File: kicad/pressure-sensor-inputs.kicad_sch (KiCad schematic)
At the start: 10 parts

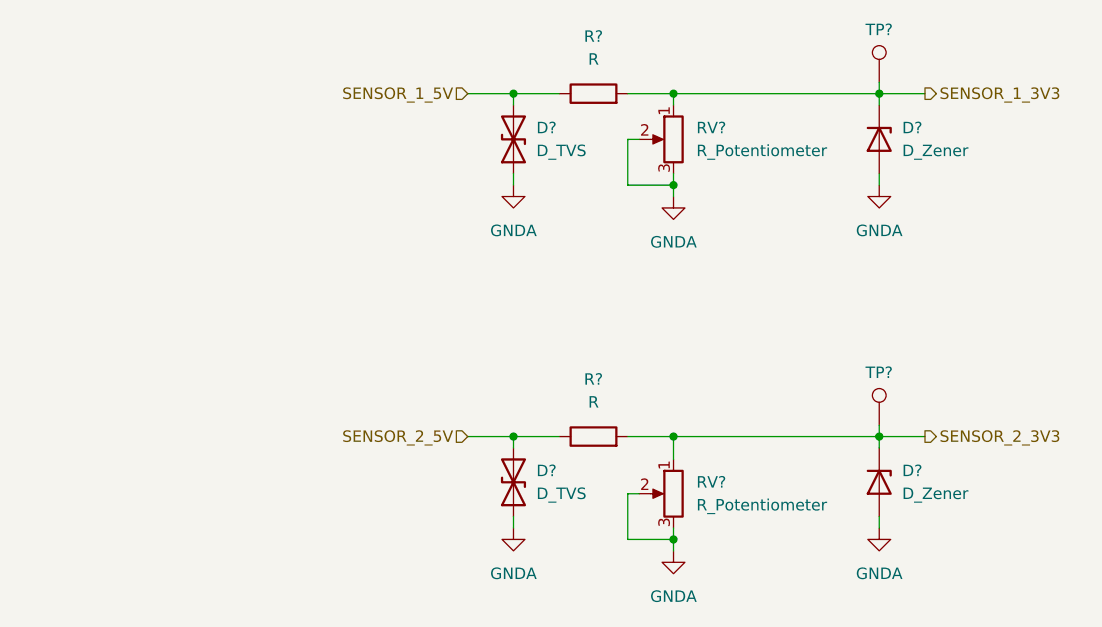
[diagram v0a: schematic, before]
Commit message: Update ADC input divider and protection
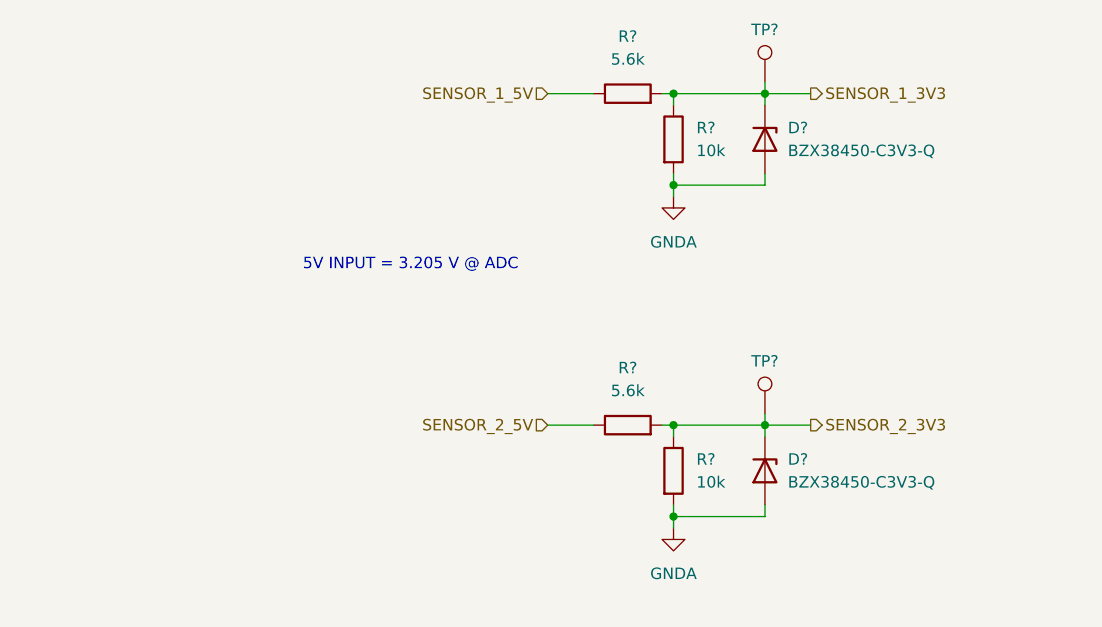
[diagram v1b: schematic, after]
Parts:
- removed D?: D_Zener, symbol symbols:D_Zener
- removed D? (x2): D_TVS, symbol bmw-e36-abs-module:D_TVS
- removed R?: R, symbol symbols:R
- removed RV? (x2): R_Potentiometer, symbol symbols:R_Potentiometer
- removed TP?: TestPoint, symbol symbols:TestPoint
- added D?: BZX38450-C3V3-Q, Diode_SMD:D_SOD-323, symbol symbols:D_Zener
- added R? (x2): 10k, symbol symbols:R
- added R?: 5.6k, symbol symbols:R
- added TP?: TestPoint, symbol symbols:TestPoint
- D?: value D_Zener -> BZX38450-C3V3-Q; footprint (none) -> Diode_SMD:D_SOD-323; Manufacturer (none) -> Nexperia; Part Number (none) -> BZX38450-C3V3-Q
- R?: value R -> 5.6k
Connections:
- net GNDA: now also D?.2 (A), R?.2, R?.2
- net SENSOR_1_3V3: now also R?.1
- net SENSOR_2_3V3: now also D?.1 (K), R?.1, R?.2, TP?.1
- net SENSOR_2_5V: now also R?.1
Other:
- note added: "5V INPUT = 3.205 V @ ADC"
- moved on the sheet: D?, R?, TP?

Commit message: Update connector; annotate and assign footprints
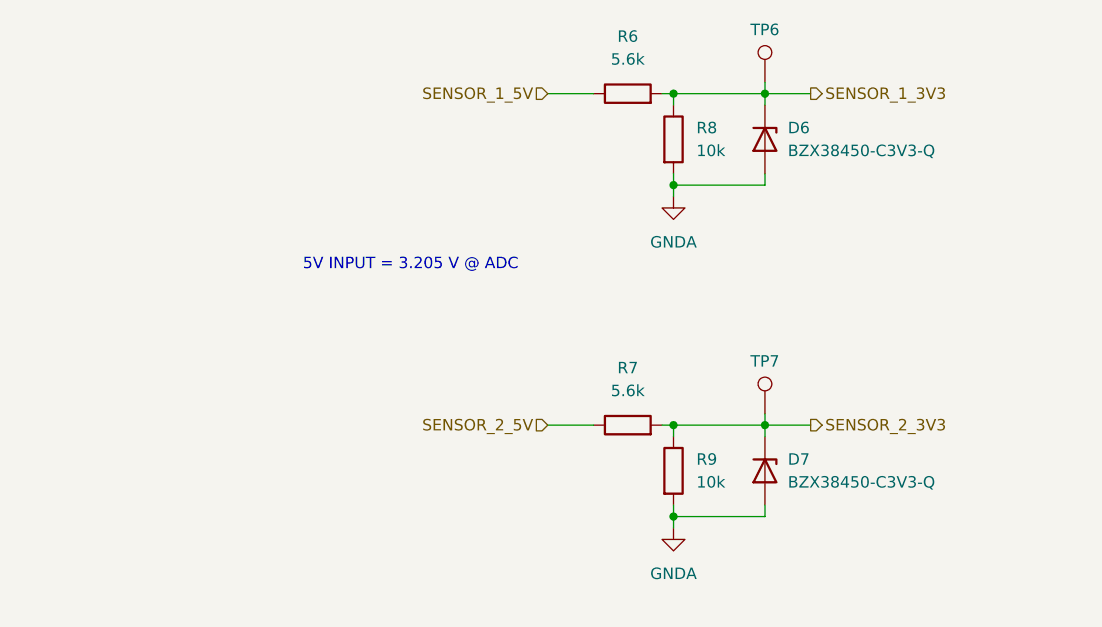
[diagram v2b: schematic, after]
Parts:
- R6, R7, R8, R9: renamed from R?; footprint (none) -> Resistor_SMD:R_0603_1608Metric
- TP6, TP7: renamed from TP?; footprint (none) -> TestPoint:TestPoint_Pad_D2.0mm
- gave numbers to parts that had none: 2
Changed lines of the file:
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@@
 		(dnp no)
 		(fields_autoplaced yes)
-		(property "Reference" "R?"
+		(property "Reference" "R8"
 			(at 208.28 111.7599 0)
 			(show_name no)
@@
 			)
 		)
-		(property "Footprint" ""
+		(property "Footprint" "Resistor_SMD:R_0603_1608Metric"
 			(at 203.962 113.03 90)
 			(hide yes)
@@
 			(project "bmw-e36-abs-adapter"
 				(path "/325be93f-b4a6-4f2b-83c3-2ccd33e5cc03/18849697-e921-4429-b50d-ca2a9ec17916"
-					(reference "R?")
+					(reference "R8")
 					(unit 1)
 				)
@@
 		(in_pos_files yes)
 		(dnp no)
-		(property "Reference" "TP?"
+		(property "Reference" "TP6"
 			(at 215.9 101.6 0)
 			(show_name no)
@@
 			)
 		)
-		(property "Footprint" ""
+		(property "Footprint" "TestPoint:TestPoint_Pad_D2.0mm"
 			(at 210.82 106.68 0)
 			(hide yes)
@@
 			(project "bmw-e36-abs-adapter"
 				(path "/325be93f-b4a6-4f2b-83c3-2ccd33e5cc03/18849697-e921-4429-b50d-ca2a9ec17916"
-					(reference "TP?")
+					(reference "TP6")
 					(unit 1)
 				)
@@
 		(dnp no)
 		(fields_autoplaced yes)
-		(property "Reference" "D?"
+		(property "Reference" "D7"
 			(at 218.44 148.5899 90)
 			(show_name no)
@@
 			(project "bmw-e36-abs-adapter"
 				(path "/325be93f-b4a6-4f2b-83c3-2ccd33e5cc03/18849697-e921-4429-b50d-ca2a9ec17916"
-					(reference "D?")
+					(reference "D7")
 					(unit 1)
 				)
@@
 		(dnp no)
 		(fields_autoplaced yes)
-		(property "Reference" "R?"
+		(property "Reference" "R9"
 			(at 208.28 148.5899 0)
 			(show_name no)
@@
 			)
 		)
-		(property "Footprint" ""
+		(property "Footprint" "Resistor_SMD:R_0603_1608Metric"
 			(at 203.962 149.86 90)
 			(hide yes)
@@
 			(project "bmw-e36-abs-adapter"
 				(path "/325be93f-b4a6-4f2b-83c3-2ccd33e5cc03/18849697-e921-4429-b50d-ca2a9ec17916"
-					(reference "R?")
+					(reference "R9")
 					(unit 1)
 				)
@@
 		(dnp no)
 		(fields_autoplaced yes)
-		(property "Reference" "R?"
+		(property "Reference" "R6"
 			(at 200.66 101.6 90)
 			(show_name no)
@@
 			)
 		)
-		(property "Footprint" ""
+		(property "Footprint" "Resistor_SMD:R_0603_1608Metric"
 			(at 200.66 109.728 90)
 			(hide yes)
@@
 			(project "bmw-e36-abs-adapter"
 				(path "/325be93f-b4a6-4f2b-83c3-2ccd33e5cc03/18849697-e921-4429-b50d-ca2a9ec17916"
-					(reference "R?")
+					(reference "R6")
 					(unit 1)
 				)
@@
 		(dnp no)
 		(fields_autoplaced yes)
-		(property "Reference" "D?"
+		(property "Reference" "D6"
 			(at 218.44 111.7599 90)
 			(show_name no)
@@
 			(project "bmw-e36-abs-adapter"
 				(path "/325be93f-b4a6-4f2b-83c3-2ccd33e5cc03/18849697-e921-4429-b50d-ca2a9ec17916"
-					(reference "D?")
+					(reference "D6")
 					(unit 1)
 				)
@@
 		(in_pos_files yes)
 		(dnp no)
-		(property "Reference" "TP?"
+		(property "Reference" "TP7"
 			(at 215.9 138.43 0)
 			(show_name no)
@@
 			)
 		)
-		(property "Footprint" ""
+		(property "Footprint" "TestPoint:TestPoint_Pad_D2.0mm"
 			(at 210.82 143.51 0)
 			(hide yes)
@@
 			(project "bmw-e36-abs-adapter"
 				(path "/325be93f-b4a6-4f2b-83c3-2ccd33e5cc03/18849697-e921-4429-b50d-ca2a9ec17916"
-					(reference "TP?")
+					(reference "TP7")
 					(unit 1)
 				)
@@
 		(dnp no)
 		(fields_autoplaced yes)
-		(property "Reference" "R?"
+		(property "Reference" "R7"
 			(at 200.66 138.43 90)
 			(show_name no)
@@
 			)
 		)
-		(property "Footprint" ""
+		(property "Footprint" "Resistor_SMD:R_0603_1608Metric"
 			(at 200.66 146.558 90)
 			(hide yes)
@@
 			(project "bmw-e36-abs-adapter"
 				(path "/325be93f-b4a6-4f2b-83c3-2ccd33e5cc03/18849697-e921-4429-b50d-ca2a9ec17916"
-					(reference "R?")
+					(reference "R7")
 					(unit 1)
 				)
@@
 		(dnp no)
 		(fields_autoplaced yes)
-		(property "Reference" "#PWR?"
+		(property "Reference" "#PWR034"
 			(at 205.74 125.73 0)
 			(hide yes)
@@
 			(project "bmw-e36-abs-adapter"
 				(path "/325be93f-b4a6-4f2b-83c3-2ccd33e5cc03/18849697-e921-4429-b50d-ca2a9ec17916"
-					(reference "#PWR?")
+					(reference "#PWR034")
 					(unit 1)
 				)
@@
 		(dnp no)
 		(fields_autoplaced yes)
-		(property "Reference" "#PWR?"
+		(property "Reference" "#PWR035"
 			(at 205.74 162.56 0)
 			(hide yes)
@@
 			(project "bmw-e36-abs-adapter"
 				(path "/325be93f-b4a6-4f2b-83c3-2ccd33e5cc03/18849697-e921-4429-b50d-ca2a9ec17916"
-					(reference "#PWR?")
-					(unit 1)
-				)
+					(reference "#PWR035")
+					(unit 1)
+				)

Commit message: Add optional RC filter to pressure sensor inputs
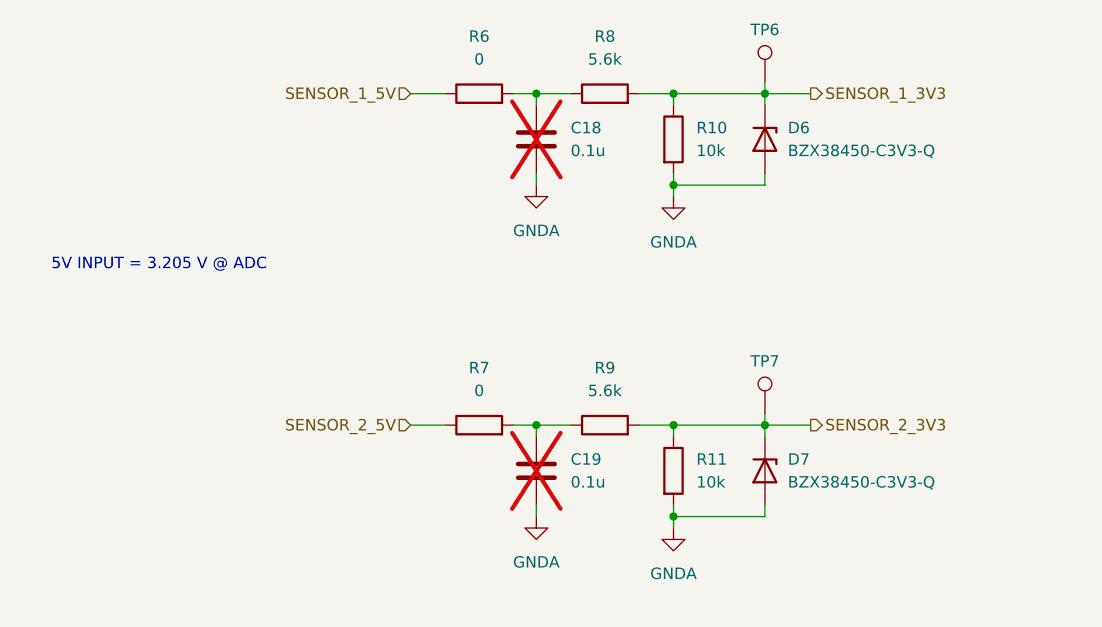
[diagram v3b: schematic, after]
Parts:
- added C18, C19: 0.1u, Capacitor_SMD:C_0603_1608Metric, symbol symbols:C
- added R6, R7: 0, Resistor_SMD:R_0603_1608Metric, symbol symbols:R
- renumbered R8 to R10, R9 to R11, R6 to R8, R7 to R9
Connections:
- net GNDA: now also C18.2, C19.2
- net SENSOR_1_5V: now also R6.1; no longer R8.1
- net SENSOR_2_5V: now also R7.1; no longer R9.1
- new net: C19.1, R7.2, R9.1
- new net: C18.1, R6.2, R8.1
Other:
- moved on the sheet: R8, R9

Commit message: Update part numbers and fix ERC issues
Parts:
- C18, C19: Manufacturer (none) -> Murata; Part Number (none) -> GCJ188R71H104KA12D; now left out of the parts list
- R10, R11: Manufacturer (none) -> Panasonic; Part Number (none) -> ERJ-3EKF1002V
- R6, R7: Manufacturer (none) -> Panasonic; Part Number (none) -> ERJ-H3G0R00V
- R8, R9: Manufacturer (none) -> Panasonic; Part Number (none) -> ERJ-3EKF5601V
- TP6, TP7: now left out of the parts list
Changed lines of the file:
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@@
+			)
+		)
+		(property "Manufacturer" "Panasonic"
+			(at 205.74 113.03 0)
+			(hide yes)
+			(show_name no)
+			(do_not_autoplace no)
+			(effects
+				(font
+					(size 1.27 1.27)
+				)
+			)
+		)
+		(property "Part Number" "ERJ-3EKF1002V"
+			(at 205.74 113.03 0)
+			(hide yes)
+			(show_name no)
+			(do_not_autoplace no)
+			(effects
+				(font
+					(size 1.27 1.27)
+				)
 			)
 		)
@@
 		(body_style 1)
 		(exclude_from_sim no)
-		(in_bom yes)
+		(in_bom no)
 		(on_board yes)
 		(in_pos_files yes)
@@
 		)
 		(property "Description" "Unpolarized capacitor"
+			(at 190.5 149.86 0)
+			(hide yes)
+			(show_name no)
+			(do_not_autoplace no)
+			(effects
+				(font
+					(size 1.27 1.27)
+				)
+			)
+		)
+		(property "Manufacturer" "Murata"
+			(at 190.5 149.86 0)
+			(hide yes)
+			(show_name no)
+			(do_not_autoplace no)
+			(effects
+				(font
+					(size 1.27 1.27)
+				)
+			)
+		)
+		(property "Part Number" "GCJ188R71H104KA12D"
 			(at 190.5 149.86 0)
 			(hide yes)
@@
 		(body_style 1)
 		(exclude_from_sim no)
-		(in_bom yes)
+		(in_bom no)
 		(on_board yes)
 		(in_pos_files yes)
@@
 		)
 		(property "Description" "Unpolarized capacitor"
+			(at 190.5 113.03 0)
+			(hide yes)
+			(show_name no)
+			(do_not_autoplace no)
+			(effects
+				(font
+					(size 1.27 1.27)
+				)
+			)
+		)
+		(property "Manufacturer" "Murata"
+			(at 190.5 113.03 0)
+			(hide yes)
+			(show_name no)
+			(do_not_autoplace no)
+			(effects
+				(font
+					(size 1.27 1.27)
+				)
+			)
+		)
+		(property "Part Number" "GCJ188R71H104KA12D"
 			(at 190.5 113.03 0)
 			(hide yes)
@@
 		(body_style 1)
 		(exclude_from_sim no)
-		(in_bom yes)
+		(in_bom no)
 		(on_board yes)
 		(in_pos_files yes)
@@
 			)
 		)
+		(property "Manufacturer" "Panasonic"
+			(at 205.74 149.86 0)
+			(hide yes)
+			(show_name no)
+			(do_not_autoplace no)
+			(effects
+				(font
+					(size 1.27 1.27)
+				)
+			)
+		)
+		(property "Part Number" "ERJ-3EKF1002V"
+			(at 205.74 149.86 0)
+			(hide yes)
+			(show_name no)
+			(do_not_autoplace no)
+			(effects
+				(font
+					(size 1.27 1.27)
+				)
+			)
+		)
 		(pin "1"
 		)
@@
 			)
 		)
+		(property "Manufacturer" "Panasonic"
+			(at 184.15 144.78 90)
+			(hide yes)
+			(show_name no)
+			(do_not_autoplace no)
+			(effects
+				(font
+					(size 1.27 1.27)
+				)
+			)
+		)
+		(property "Part Number" "ERJ-H3G0R00V"
+			(at 184.15 144.78 90)
+			(hide yes)
+			(show_name no)
+			(do_not_autoplace no)
+			(effects
+				(font
+					(size 1.27 1.27)
+				)
+			)
+		)
 		(pin "2"
 		)
@@
 			)
 		)
+		(property "Manufacturer" "Panasonic"
+			(at 198.12 107.95 90)
+			(hide yes)
+			(show_name no)
+			(do_not_autoplace no)
+			(effects
+				(font
+					(size 1.27 1.27)
+				)
+			)
+		)
+		(property "Part Number" "ERJ-3EKF5601V"
+			(at 198.12 107.95 90)
+			(hide yes)
+			(show_name no)
+			(do_not_autoplace no)
+			(effects
+				(font
+					(size 1.27 1.27)
+				)
+			)
+		)
 		(pin "2"
 		)
@@
 		(body_style 1)
 		(exclude_from_sim no)
-		(in_bom yes)
+		(in_bom no)
 		(on_board yes)
 		(in_pos_files yes)
@@
 			)
 		)
+		(property "Manufacturer" "Panasonic"
+			(at 198.12 144.78 90)
+			(hide yes)
+			(show_name no)
+			(do_not_autoplace no)
+			(effects
+				(font
+					(size 1.27 1.27)
+				)
+			)
+		)
+		(property "Part Number" "ERJ-3EKF5601V"
+			(at 198.12 144.78 90)
+			(hide yes)
+			(show_name no)
+			(do_not_autoplace no)
+			(effects
+				(font
+					(size 1.27 1.27)
+				)
+			)
+		)
 		(pin "2"
 		)
@@
 			(hide yes)
 			(show_name no)
+			(do_not_autoplace no)
+			(effects
+				(font
+					(size 1.27 1.27)
+				)
+			)
+		)
+		(property "Manufacturer" "Panasonic"
+			(at 184.15 107.95 90)
+			(hide yes)
+			(show_name no)
+			(do_not_autoplace no)
+			(effects
+				(font
+					(size 1.27 1.27)
+				)
+			)
+		)
+		(property "Part Number" "ERJ-H3G0R00V"
+			(at 184.15 107.95 90)
+			(hide yes)
+			(show_name no)

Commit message: Initial placement on PCB
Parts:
- TP6, TP7: footprint TestPoint:TestPoint_Pad_D2.0mm -> TestPoint:TestPoint_Pad_D1.5mm
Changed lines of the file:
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@@
 			)
 		)
-		(property "Footprint" "TestPoint:TestPoint_Pad_D2.0mm"
+		(property "Footprint" "TestPoint:TestPoint_Pad_D1.5mm"
 			(at 210.82 106.68 0)
 			(hide yes)
@@
 			)
 		)
-		(property "Footprint" "TestPoint:TestPoint_Pad_D2.0mm"
+		(property "Footprint" "TestPoint:TestPoint_Pad_D1.5mm"
 			(at 210.82 143.51 0)
 			(hide yes)
